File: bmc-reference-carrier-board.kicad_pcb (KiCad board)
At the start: 2 copper layers, 120.4 x 90 mm, 1 part, among them J1 PCB-Edge_DC-SCM-2.1_2x84_Rev-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

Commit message: [#81876] Add 8L stackup definition
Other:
- copper layers 2 -> 8
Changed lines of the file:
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@@
 	(generator_version "9.0")
 	(general
-		(thickness 1.6)
+		(thickness 1.62)
 		(legacy_teardrops no)
 	)
@@
 	(layers
 		(0 "F.Cu" signal)
+		(4 "In1.Cu" signal)
+		(6 "In2.Cu" signal)
+		(8 "In3.Cu" signal)
+		(10 "In4.Cu" jumper)
+		(12 "In5.Cu" signal)
+		(14 "In6.Cu" signal)
 		(2 "B.Cu" signal)
 		(9 "F.Adhes" user "F.Adhesive")
@@
 		(43 "User.3" user)
 		(45 "User.4" user)
+		(47 "User.5" user)
+		(49 "User.6" user)
+		(51 "User.7" user)
+		(53 "User.8" user)
+		(55 "User.9" user "overlay")
 	)
 	(setup
+		(stackup
+			(layer "F.SilkS"
+				(type "Top Silk Screen")
+				(color "White")
+			)
+			(layer "F.Paste"
+				(type "Top Solder Paste")
+			)
+			(layer "F.Mask"
+				(type "Top Solder Mask")
+				(color "Black")
+				(thickness 0.01)
+			)
+			(layer "F.Cu"
+				(type "copper")
+				(thickness 0.035)
+			)
+			(layer "dielectric 1"
+				(type "prepreg")
+				(thickness 0.12)
+				(material "PR2116")
+				(epsilon_r 4.3)
+				(loss_tangent 0.02)
+			)
+			(layer "In1.Cu"
+				(type "copper")
+				(thickness 0.035)
+			)
+			(layer "dielectric 2"
+				(type "core")
+				(thickness 0.2)
+				(material "FR4")
+				(epsilon_r 4.39)
+				(loss_tangent 0.02)
+			)
+			(layer "In2.Cu"
+				(type "copper")
+				(thickness 0.035)
+			)
+			(layer "dielectric 3"
+				(type "prepreg")
+				(thickness 0.12)
+				(material "PR2116")
+				(epsilon_r 4.39)
+				(loss_tangent 0.02) addsublayer
+				(thickness 0.12)
+				(material "PR2116")
+				(epsilon_r 4.39)
+				(loss_tangent 0)
+			)
+			(layer "In3.Cu"
+				(type "copper")
+				(thickness 0.035)
+			)
+			(layer "dielectric 4"
+				(type "core")
+				(thickness 0.2)
+				(material "FR4")
+				(epsilon_r 4.39)
+				(loss_tangent 0.02)
+			)
+			(layer "In4.Cu"
+				(type "copper")
+				(thickness 0.035)
+			)
+			(layer "dielectric 5"
+				(type "prepreg")
+				(thickness 0.12)
+				(material "PR2116")
+				(epsilon_r 4.39)
+				(loss_tangent 0.02) addsublayer
+				(thickness 0.12)
+				(material "PR2116")
+				(epsilon_r 4.39)
+				(loss_tangent 0)
+			)
+			(layer "In5.Cu"
+				(type "copper")
+				(thickness 0.035)
+			)
+			(layer "dielectric 6"
+				(type "core")
+				(thickness 0.2)
+				(material "FR4")
+				(epsilon_r 4.39)
+				(loss_tangent 0.02)
+			)
+			(layer "In6.Cu"
+				(type "copper")
+				(thickness 0.035)
+			)
+			(layer "dielectric 7"
+				(type "prepreg")
+				(thickness 0.12)
+				(material "PR2116")
+				(epsilon_r 4.3)
+				(loss_tangent 0.02)
+			)
+			(layer "B.Cu"
+				(type "copper")
+				(thickness 0.035)
+			)
+			(layer "B.Mask"
+				(type "Bottom Solder Mask")
+				(color "Black")
+				(thickness 0.01)
+			)
+			(layer "B.Paste"
+				(type "Bottom Solder Paste")
+			)
+			(layer "B.SilkS"
+				(type "Bottom Silk Screen")
+				(color "White")
+			)
+			(copper_finish "ENIG")
+			(dielectric_constraints no)
+		)
 		(pad_to_mask_clearance 0)
 		(allow_soldermask_bridges_in_footprints no)

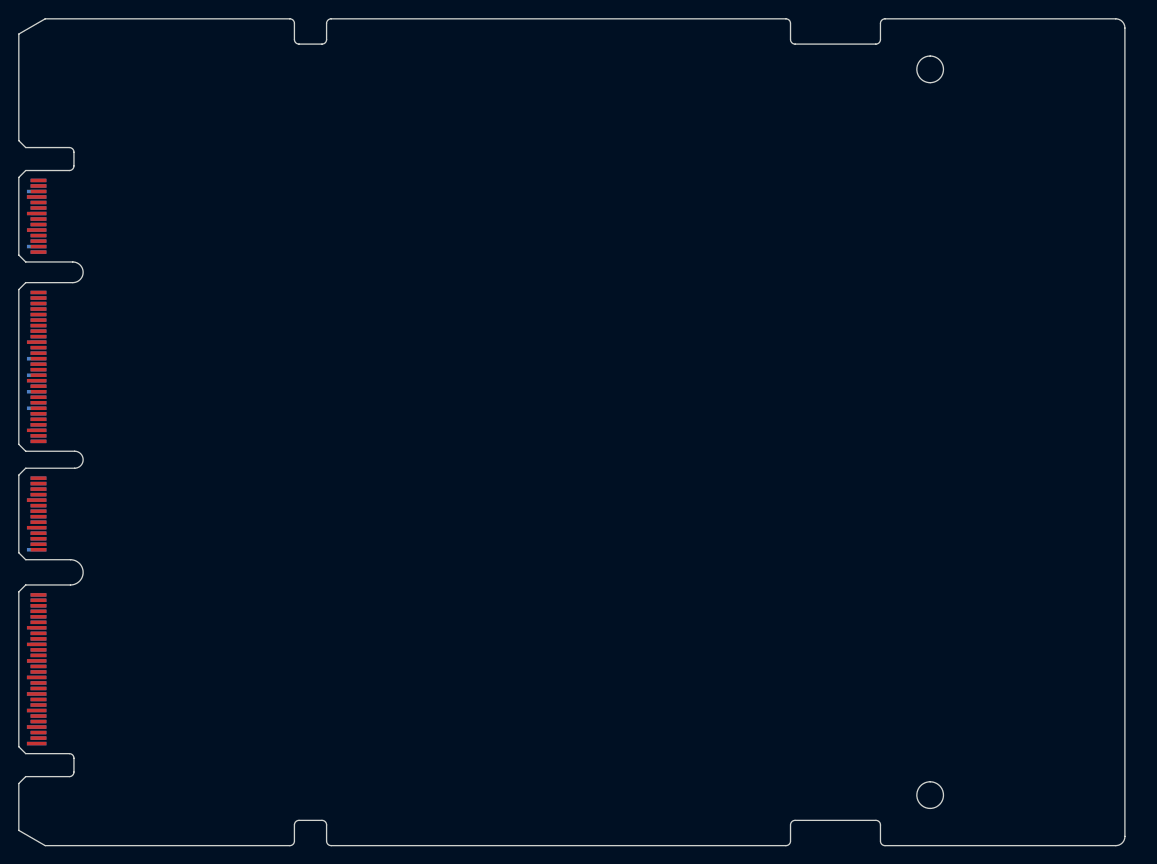
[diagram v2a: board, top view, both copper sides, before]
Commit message: [#82176] Add Ethernet connections
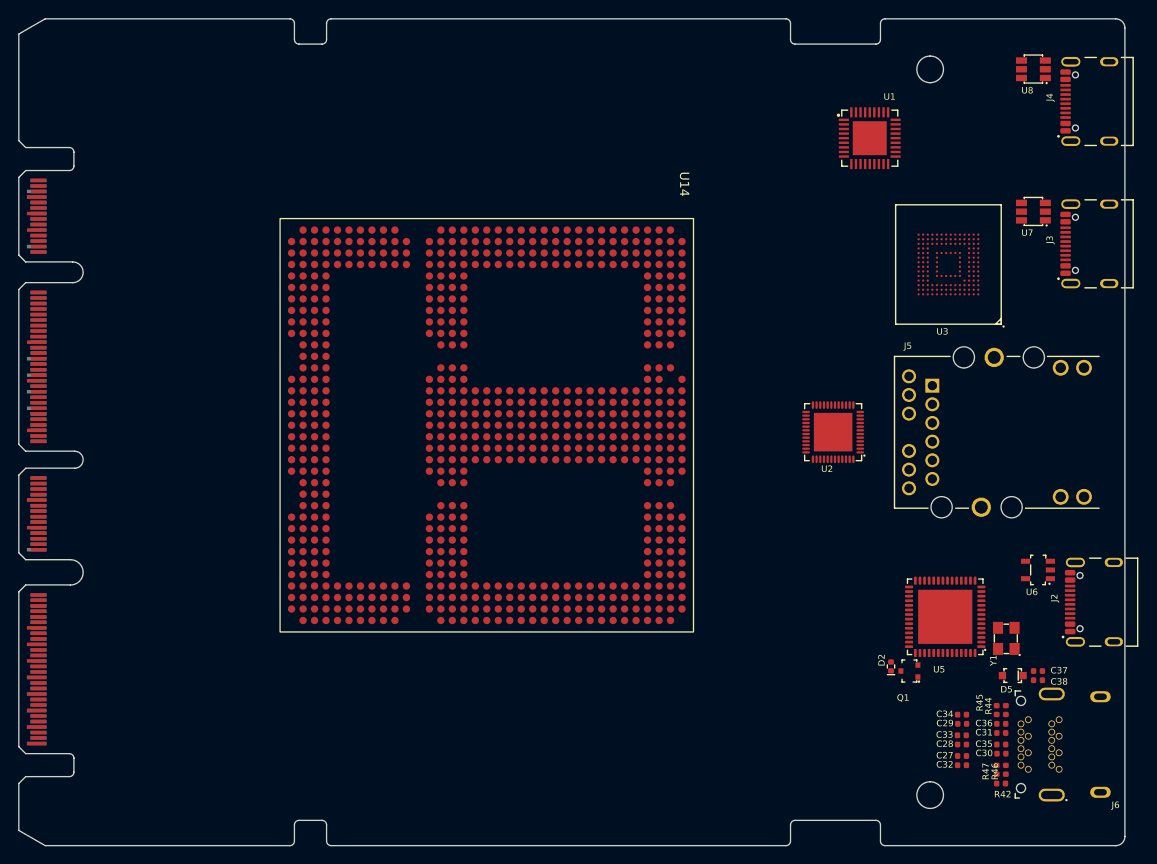
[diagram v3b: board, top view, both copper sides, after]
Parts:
- added C27: C_100n_0402, antmicro-footprints:C_0402_1005Metric, F.Cu at (197.7, 121.2)
- added C28: C_100n_0402, antmicro-footprints:C_0402_1005Metric, F.Cu at (197.7, 120.0)
- added C29: C_100n_0402, antmicro-footprints:C_0402_1005Metric, F.Cu at (197.8, 117.8)
- added C30: C_100n_0402, antmicro-footprints:C_0402_1005Metric, F.Cu at (202.0, 121.0)
- added C31: C_100n_0402, antmicro-footprints:C_0402_1005Metric, F.Cu at (202.0, 118.8)
- added C32: C_100n_0402, antmicro-footprints:C_0402_1005Metric, F.Cu at (197.7, 122.2)
- added C33: C_100n_0402, antmicro-footprints:C_0402_1005Metric, F.Cu at (197.7, 119.0)
- added C34: C_100n_0402, antmicro-footprints:C_0402_1005Metric, F.Cu at (197.7, 116.8)
- added C35: C_100n_0402, antmicro-footprints:C_0402_1005Metric, F.Cu at (202.0, 120.0)
- added C36: C_100n_0402, antmicro-footprints:C_0402_1005Metric, F.Cu at (202.0, 117.8)
- added C37: C_4u7_6.3V_0402, antmicro-footprints:C_0402_1005Metric, F.Cu at (206.0, 112.0)
- added C38: C_4u7_6.3V_0402, antmicro-footprints:C_0402_1005Metric, F.Cu at (206.0, 113.0)
- added D2: LED_G_0402_VLMTG1500-GS08, antmicro-footprints:LED_0402_1005Metric_G, F.Cu at (190.0, 111.5)
- added D5: 1N4148WS-7-F, antmicro-footprints:D_SOD-323, F.Cu at (203.2, 112.5)
- added J2: USB-C_GCT_USB4105-GF-A, antmicro-footprints:USB-C_Receptacle_GCT_USB4105-GF-A, F.Cu at (213.0, 104.5)
- added J3: USB-C_GCT_USB4105-GF-A, antmicro-footprints:USB-C_Receptacle_GCT_USB4105-GF-A, F.Cu at (212.5, 65.5)
- added J4: USB-C_GCT_USB4105-GF-A, antmicro-footprints:USB-C_Receptacle_GCT_USB4105-GF-A, F.Cu at (212.5, 50.0)
- added J5: L834-1G1T-S7, antmicro-footprints:RJ45_BEL_L834-1G1T-S7, F.Cu at (194.5, 80.9)
- added J6: DisplayPort-Mini_TE_2129320-3, antmicro-footprints:DisplayPort-Mini_Receptacle_TE_2129320-3, F.Cu at (208.3, 122.7)
- added Q1: BSS84AKW, antmicro-footprints:SOT-323, F.Cu at (192.0, 112.0)
- added R42: R_51k_0402, antmicro-footprints:R_0402_1005Metric, F.Cu at (202.0, 124.2)
- added R44: R_100k_0402, antmicro-footprints:R_0402_1005Metric, F.Cu at (202.5, 116.2)
- added R45: R_100k_0402, antmicro-footprints:R_0402_1005Metric, F.Cu at (201.5, 116.2)
- added R46: R_1M_0402, antmicro-footprints:R_0402_1005Metric, F.Cu at (202.5, 122.8)
- added R47: R_1M_0402, antmicro-footprints:R_0402_1005Metric, F.Cu at (201.5, 122.8)
- added U1: USB2514B-I_M2, antmicro-footprints:QFN-36-1EP_6x6mm_P0.5mm_EP3.7x3.7mm, F.Cu at (187.7, 54.0)
- added U14: OSM-L_Carrier-side, antmicro-footprints:OSM-L_Carrier-side, F.Cu at (168.5, 62.8)
- added U2: RTL8211FS-CG, antmicro-footprints:QFN-48-1EP_6x6mm, F.Cu at (183.7, 86.0)
- added U3: SDINBDG4-8G, antmicro-footprints:BGA-196-153_11.5x13mm_Layout14x14_P0.5x0.5mm, F.Cu at (196.2, 67.7)
- added U5: FT4232H_VQFN, antmicro-footprints:QFN-56-1EP_8x8mm_P0.5mm, F.Cu at (195.9, 106.1)
- added U6: NCP718BSN330T1G, antmicro-footprints:SOT-23-5, F.Cu at (206.0, 101.0)
- added U7: AP22615A_TSOT26, antmicro-footprints:TSOT23-6, F.Cu at (205.5, 62.0)
- added U8: AP22615A_TSOT26, antmicro-footprints:TSOT23-6, F.Cu at (205.5, 46.5)
- added Y1: Resonator_12MHz_ABM8G, antmicro-footprints:Resonator_SMD_Abracon_ABM8G_3.2x2.5mm, F.Cu at (202.5, 108.5)
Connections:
- net Net-(J1A-GND-PadA19) renamed GND
- net Net-(J1A-P12V_AUX-PadA1) renamed /DC-SCM 2.1 connector/DC_SCM_12V_AUX
- J1 pad A13: unconnected-(J1A-SCM_HPM_STBY_RST_N-PadA13) -> /DC-SCM 2.1 connector/DC_SCM_STBY_RST_N
- J1 pad A14: unconnected-(J1A-SCM_HPM_STBY_EN-PadA14) -> /DC-SCM 2.1 connector/DC_SCM_STBY_EN
- J1 pad A7: unconnected-(J1A-PRSNT1_HPM_SCM_N-PadA7) -> /DC-SCM 2.1 connector/DC_SCM_PRSNT0_N
- J1 pad B26: unconnected-(J1A-HPM_SCM_STBY_RDY-PadB26) -> /DC-SCM 2.1 connector/DC_SCM_STBY_RDY
- J1 pad B27: unconnected-(J1A-HPM_SCM_INTRUSION_N-PadB27) -> /DC-SCM 2.1 connector/DC_SCM_INTRUSION_N
- J1 pad B28: unconnected-(J1A-P3V0_HPM_SCM_BAT-PadB28) -> /DC-SCM 2.1 connector/DC_SCM_P3V0
- J1 pad B58: unconnected-(J1A-PRSNT0_SCM_HPM_N-PadB58) -> /DC-SCM 2.1 connector/DC_SCM_PRSNT0_N

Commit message: [#82176] Import components from schematic and create initial placement
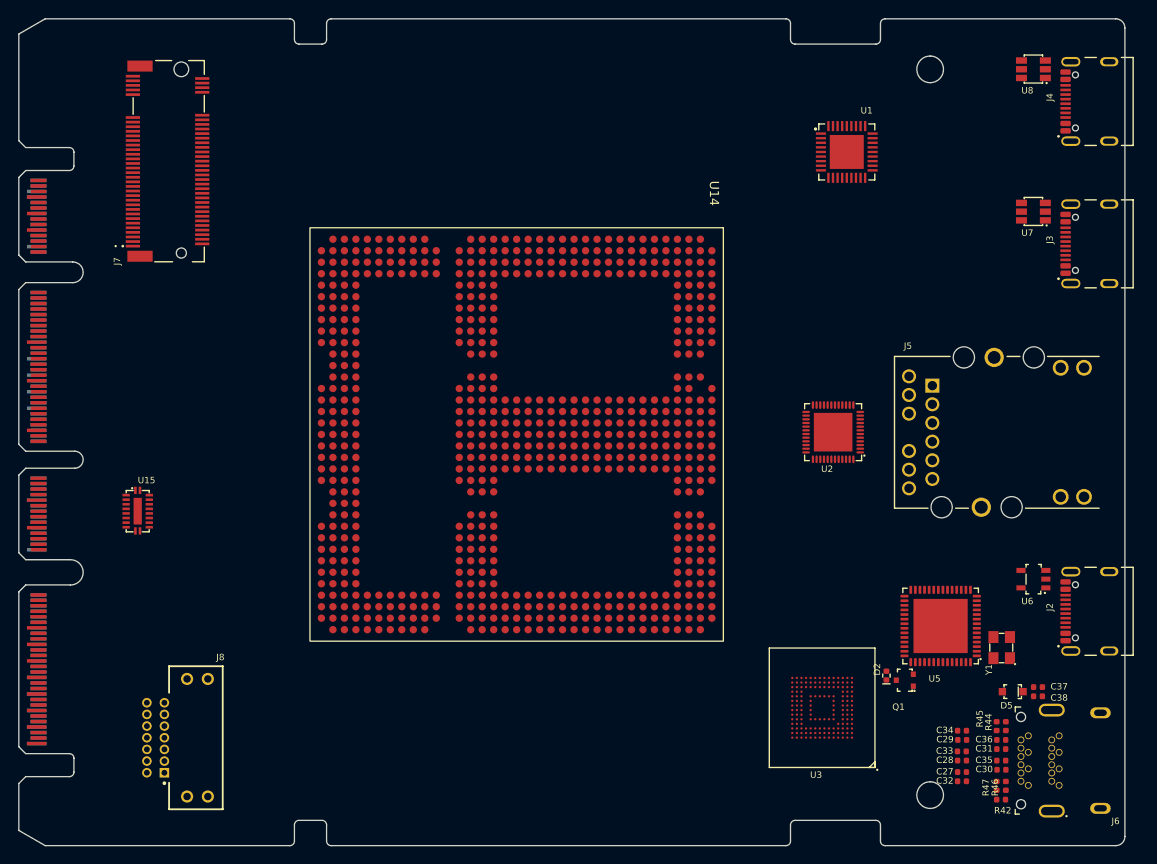
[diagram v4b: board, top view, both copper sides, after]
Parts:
- added J7: Bus_M.2_1-2199230-6, antmicro-footprints:Bus_M.2_Socket_Key_M_TE_1-2199230-6, F.Cu at (111.2, 56.5)
- added J8: TFM-107-01-X-D-RE1-WT, antmicro-footprints:Socket_Samtec_TFM_2x7_TFM-107-01-X-D-RE1-WT, F.Cu at (110.0, 119.3)
- added U15: CBTL02043ABQ, antmicro-footprints:DHVQFN-20-1EP_2.5x4.5_P0.5mm, F.Cu at (108.0, 94.6)
- moved U3 50.2 mm to (182.5, 116.0)
- moved U14 3.40 mm to (171.8, 63.8)
- moved U1 2.92 mm to (185.2, 55.5)
- moved C27 1.75 mm to (197.7, 123.0)
- moved C28 1.75 mm to (197.7, 121.8)
- moved C29 1.75 mm to (197.8, 119.5)
- moved C30 1.75 mm to (202.0, 122.8)
- moved C31 1.75 mm to (202.0, 120.5)
- moved C32 1.75 mm to (197.7, 124.0)
- moved C33 1.75 mm to (197.7, 120.8)
- moved C34 1.75 mm to (197.7, 118.5)
- moved C35 1.75 mm to (202.0, 121.8)
- moved C36 1.75 mm to (202.0, 119.5)
- moved C37 1.75 mm to (206.0, 113.8)
- moved C38 1.75 mm to (206.0, 114.8)
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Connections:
- U2 pad 10: /Ethernet PHY/ETHERNET.MDI3+ -> unconnected-(U2D-MDIP3-Pad10)
- U2 pad 11: /Ethernet PHY/ETHERNET.MDI3- -> unconnected-(U2D-MDIN3-Pad11)
- U2 pad 2: /Ethernet PHY/ETHERNET.MDI0+ -> unconnected-(U2D-MDIP0-Pad2)
- U2 pad 3: /Ethernet PHY/ETHERNET.MDI0- -> unconnected-(U2D-MDIN0-Pad3)
- U2 pad 5: /Ethernet PHY/ETHERNET.MDI1+ -> unconnected-(U2D-MDIP1-Pad5)
- U2 pad 6: /Ethernet PHY/ETHERNET.MDI1- -> unconnected-(U2D-MDIN1-Pad6)
- U2 pad 7: /Ethernet PHY/ETHERNET.MDI2+ -> unconnected-(U2D-MDIP2-Pad7)
- U2 pad 8: /Ethernet PHY/ETHERNET.MDI2- -> unconnected-(U2D-MDIN2-Pad8)

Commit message: [#82176] Add M.2 standoff, update placement
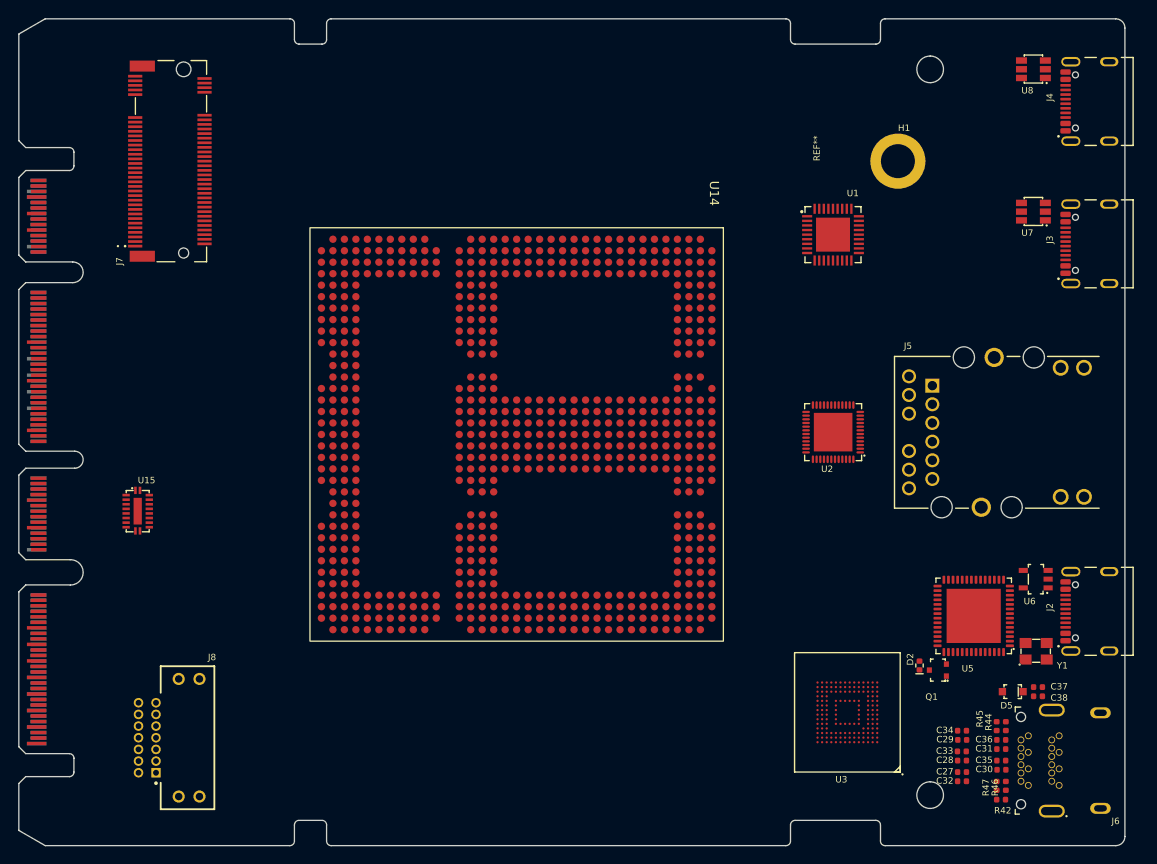
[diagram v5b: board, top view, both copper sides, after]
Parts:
- added H1: Spacer_Drill3.7mm_H2.5mm_9774025151R, antmicro-footprints:Spacer_Drill3.7mm_H2.5mm_9774025151R, F.Cu at (190.8, 56.5)
- added REF**: Mech_M2_2280_H2.5mm, antmicro-footprints:Mech_M2_2280_H2.5mm, F.Cu at (191.2, 56.5)
- moved U1 9.12 mm to (183.7, 64.5)
- moved D2 3.77 mm to (193.1, 111.4)
- moved Q1 3.77 mm to (195.1, 111.9)
- moved U5 3.77 mm to (199.0, 106.0)
- moved Y1 3.76 mm to (205.8, 109.8), turned to 0 degrees
- moved U3 2.79 mm to (185.2, 116.5)
- moved J8 0.91 mm to (109.0, 119.3)
- moved J7 0.25 mm to (111.5, 56.5)
- moved U6 0.25 mm to (205.8, 102.0)
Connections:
- U2 pad 10: unconnected-(U2D-MDIP3-Pad10) -> /Ethernet PHY/ETHERNET.MDI3+
- U2 pad 11: unconnected-(U2D-MDIN3-Pad11) -> /Ethernet PHY/ETHERNET.MDI3-
- U2 pad 2: unconnected-(U2D-MDIP0-Pad2) -> /Ethernet PHY/ETHERNET.MDI0+
- U2 pad 3: unconnected-(U2D-MDIN0-Pad3) -> /Ethernet PHY/ETHERNET.MDI0-
- U2 pad 5: unconnected-(U2D-MDIP1-Pad5) -> /Ethernet PHY/ETHERNET.MDI1+
- U2 pad 6: unconnected-(U2D-MDIN1-Pad6) -> /Ethernet PHY/ETHERNET.MDI1-
- U2 pad 7: unconnected-(U2D-MDIP2-Pad7) -> /Ethernet PHY/ETHERNET.MDI2+
- U2 pad 8: unconnected-(U2D-MDIN2-Pad8) -> /Ethernet PHY/ETHERNET.MDI2-
